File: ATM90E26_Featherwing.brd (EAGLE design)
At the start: 50.8 x 39.4 mm, 56 parts, among them J1 ST-PJ-312, J2 4P-SMD-2.0-90D, J3 4P-SMD-2.0-90D, J4 12V AC, Q1 8.192MHz, U1 ATM90E26, U2 CJT1117-5.0-SOT223

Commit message: Applied hackvana DRU
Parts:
- moved CS 0.25 mm to (3.30, 8.64)
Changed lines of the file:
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@@
 <?xml version="1.0" encoding="utf-8"?>
 <!DOCTYPE eagle SYSTEM "eagle.dtd">
-<eagle version="7.4.0">
+<eagle version="7.6.0">
 <drawing>
 <settings>
@@
 </class>
 </classes>
-<designrules name="OSHPark_2layer">
-<description language="de">&lt;b&gt;EAGLE Design Rules&lt;/b&gt;
+<designrules name="hackvana">
+<description language="de">&lt;b&gt;EAGLE Design Rules für Hackvana&lt;/b&gt;
 &lt;p&gt;
 Die Standard-Design-Rules sind so gewählt, dass sie für
@@
 Einstellungen hier und speichern die Design Rules unter
 einem neuen Namen ab.</description>
-<description language="en">&lt;b&gt;Laen's PCB Order Design Rules&lt;/b&gt;
+<description language="en">&lt;b&gt;EAGLE Design Rules for Hackvana&lt;/b&gt;
 &lt;p&gt;
-Please make sure your boards conform to these design rules.</description>
+The default Design Rules have been set to cover
+a wide range of applications. Your particular design
+may have different requirements, so please make the
+necessary adjustments and save your customized
+design rules under a new name.</description>
+<description language="zh">&lt;b&gt;EAGLE Design Rules for Hackvana&lt;/b&gt;
+</description>
 <param name="layerSetup" value="(1*16)"/>
-<param name="mtCopper" value="0.0356mm 0.0356mm 0.0356mm 0.0356mm 0.0356mm 0.0356mm 0.0356mm 0.0356mm 0.0356mm 0.0356mm 0.0356mm 0.0356mm 0.0356mm 0.0356mm 0.0356mm 0.0356mm"/>
-<param name="mtIsolate" value="1.5011mm 0.1499mm 0.2007mm 0.1499mm 0.2007mm 0.1499mm 0.2007mm 0.1499mm 0.2007mm 0.1499mm 0.2007mm 0.1499mm 0.2007mm 0.1499mm 0.2007mm"/>
+<param name="mtCopper" value="0.035mm 0.035mm 0.035mm 0.035mm 0.035mm 0.035mm 0.035mm 0.035mm 0.035mm 0.035mm 0.035mm 0.035mm 0.035mm 0.035mm 0.035mm 0.035mm"/>
+<param name="mtIsolate" value="1.5mm 0.15mm 0.2mm 0.15mm 0.2mm 0.15mm 0.2mm 0.15mm 0.2mm 0.15mm 0.2mm 0.15mm 0.2mm 0.15mm 0.2mm"/>
 <param name="mdWireWire" value="6mil"/>
 <param name="mdWirePad" value="6mil"/>
@@
 <param name="mdPadVia" value="6mil"/>
 <param name="mdViaVia" value="6mil"/>
-<param name="mdSmdPad" value="6mil"/>
-<param name="mdSmdVia" value="6mil"/>
-<param name="mdSmdSmd" value="6mil"/>
+<param name="mdSmdPad" value="0mil"/>
+<param name="mdSmdVia" value="0mil"/>
+<param name="mdSmdSmd" value="0mil"/>
 <param name="mdViaViaSameLayer" value="8mil"/>
 <param name="mnLayersViaInSmd" value="2"/>
-<param name="mdCopperDimension" value="15mil"/>
+<param name="mdCopperDimension" value="6mil"/>
 <param name="mdDrill" value="6mil"/>
 <param name="mdSmdStop" value="0mil"/>
 <param name="msWidth" value="6mil"/>
-<param name="msDrill" value="13mil"/>
-<param name="msMicroVia" value="13mil"/>
+<param name="msDrill" value="0.3mm"/>
+<param name="msMicroVia" value="0.25mm"/>
 <param name="msBlindViaRatio" value="0.5"/>
 <param name="rvPadTop" value="0.25"/>
@@
 <param name="rvMicroViaOuter" value="0.25"/>
 <param name="rvMicroViaInner" value="0.25"/>
-<param name="rlMinPadTop" value="7mil"/>
+<param name="rlMinPadTop" value="10mil"/>
 <param name="rlMaxPadTop" value="20mil"/>
-<param name="rlMinPadInner" value="7mil"/>
+<param name="rlMinPadInner" value="10mil"/>
 <param name="rlMaxPadInner" value="20mil"/>
-<param name="rlMinPadBottom" value="7mil"/>
+<param name="rlMinPadBottom" value="10mil"/>
 <param name="rlMaxPadBottom" value="20mil"/>
-<param name="rlMinViaOuter" value="7mil"/>
+<param name="rlMinViaOuter" value="6mil"/>
 <param name="rlMaxViaOuter" value="20mil"/>
-<param name="rlMinViaInner" value="7mil"/>
+<param name="rlMinViaInner" value="6mil"/>
 <param name="rlMaxViaInner" value="20mil"/>
 <param name="rlMinMicroViaOuter" value="4mil"/>
@@
 <param name="psTop" value="-1"/>
 <param name="psBottom" value="-1"/>
-<param name="psFirst" value="-1"/>
+<param name="psFirst" value="0"/>
 <param name="psElongationLong" value="100"/>
 <param name="psElongationOffset" value="100"/>
 <param name="mvStopFrame" value="1"/>
 <param name="mvCreamFrame" value="0"/>
-<param name="mlMinStopFrame" value="3mil"/>
-<param name="mlMaxStopFrame" value="3mil"/>
+<param name="mlMinStopFrame" value="2mil"/>
+<param name="mlMaxStopFrame" value="2mil"/>
 <param name="mlMinCreamFrame" value="0mil"/>
 <param name="mlMaxCreamFrame" value="0mil"/>
-<param name="mlViaStopLimit" value="20mil"/>
+<param name="mlViaStopLimit" value="100mil"/>
 <param name="srRoundness" value="0"/>
 <param name="srMinRoundness" value="0mil"/>
@@
 <param name="checkAngle" value="0"/>
 <param name="checkFont" value="1"/>
-<param name="checkRestrict" value="1"/>
+<param name="checkRestrict" value="0"/>
 <param name="useDiameter" value="13"/>
 <param name="maxErrors" value="50"/>
@@
 <attribute name="NAME" x="5.22" y="11.138" size="0.8" layer="26" font="vector" ratio="20" rot="MR180"/>
 </element>
-<element name="CS" library="wirepad" package="SMD1,27-2,54" value="WIREPADSMD1,27-254" x="3.302" y="8.382" smashed="yes" rot="MR90">
-<attribute name="VALUE" x="3.302" y="8.382" size="0.8" layer="28" rot="MR90"/>
-<attribute name="NAME" x="5.474" y="8.852" size="0.8" layer="26" font="vector" ratio="20" rot="MR180"/>
+<element name="CS" library="wirepad" package="SMD1,27-2,54" value="WIREPADSMD1,27-254" x="3.302" y="8.636" smashed="yes" rot="MR90">
+<attribute name="VALUE" x="3.302" y="8.636" size="0.8" layer="28" rot="MR90"/>
+<attribute name="NAME" x="5.474" y="9.106" size="0.8" layer="26" font="vector" ratio="20" rot="MR180"/>
 </element>
 <element name="C16" library="Discrete" package="C0603" value="100n" x="12.446" y="37.084" smashed="yes">
@@
 <wire x1="5.2832" y1="8.2296" x2="8.3312" y2="5.1816" width="0.254" layer="16"/>
 <wire x1="3.4544" y1="8.2296" x2="5.2832" y2="8.2296" width="0.254" layer="16"/>
-<wire x1="3.302" y1="8.382" x2="3.4544" y2="8.2296" width="0.254" layer="16"/>
+<wire x1="3.302" y1="8.636" x2="3.4544" y2="8.2296" width="0.254" layer="16"/>
 <wire x1="27.7368" y1="15.5448" x2="27.786" y2="15.595" width="0.254" layer="1"/>
 <via x="25.6032" y="11.3792" extent="1-16" drill="0.3302"/>

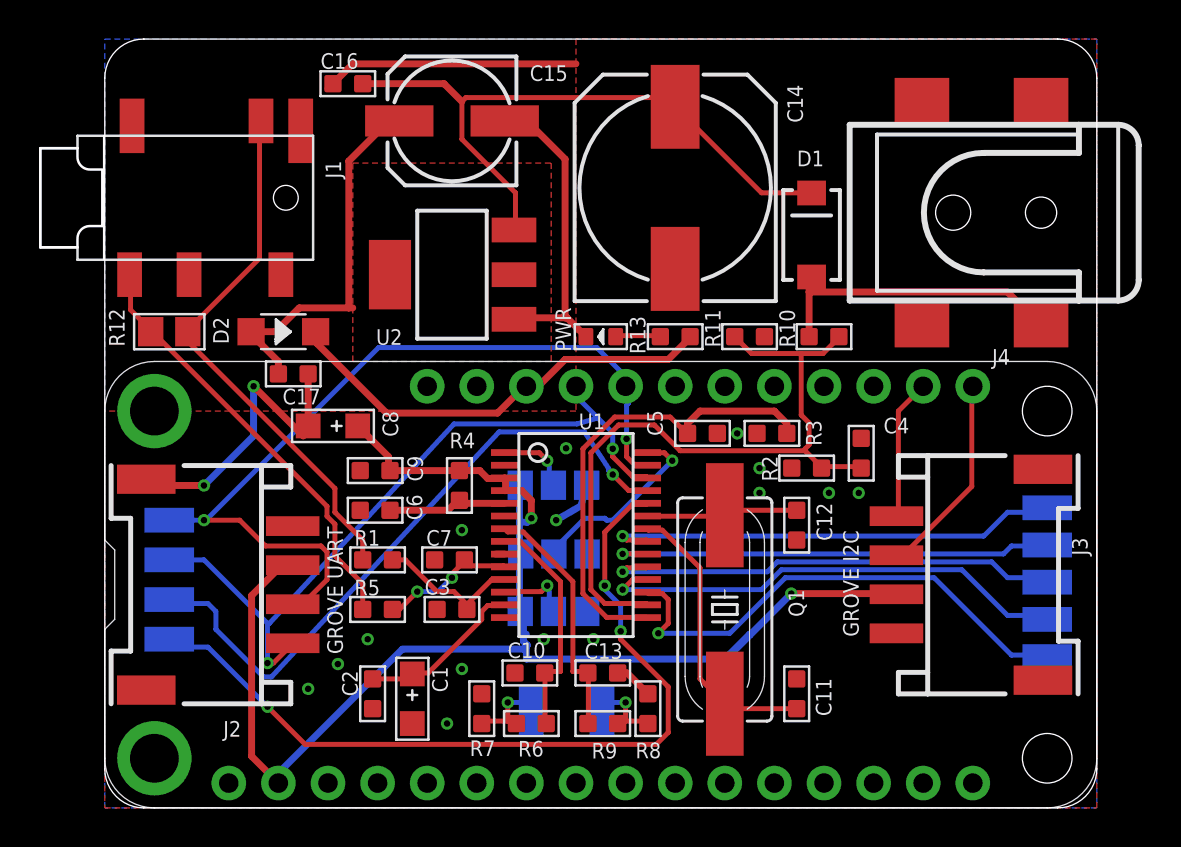
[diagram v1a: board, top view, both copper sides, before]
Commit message: Reduced size a bit to reduce cost
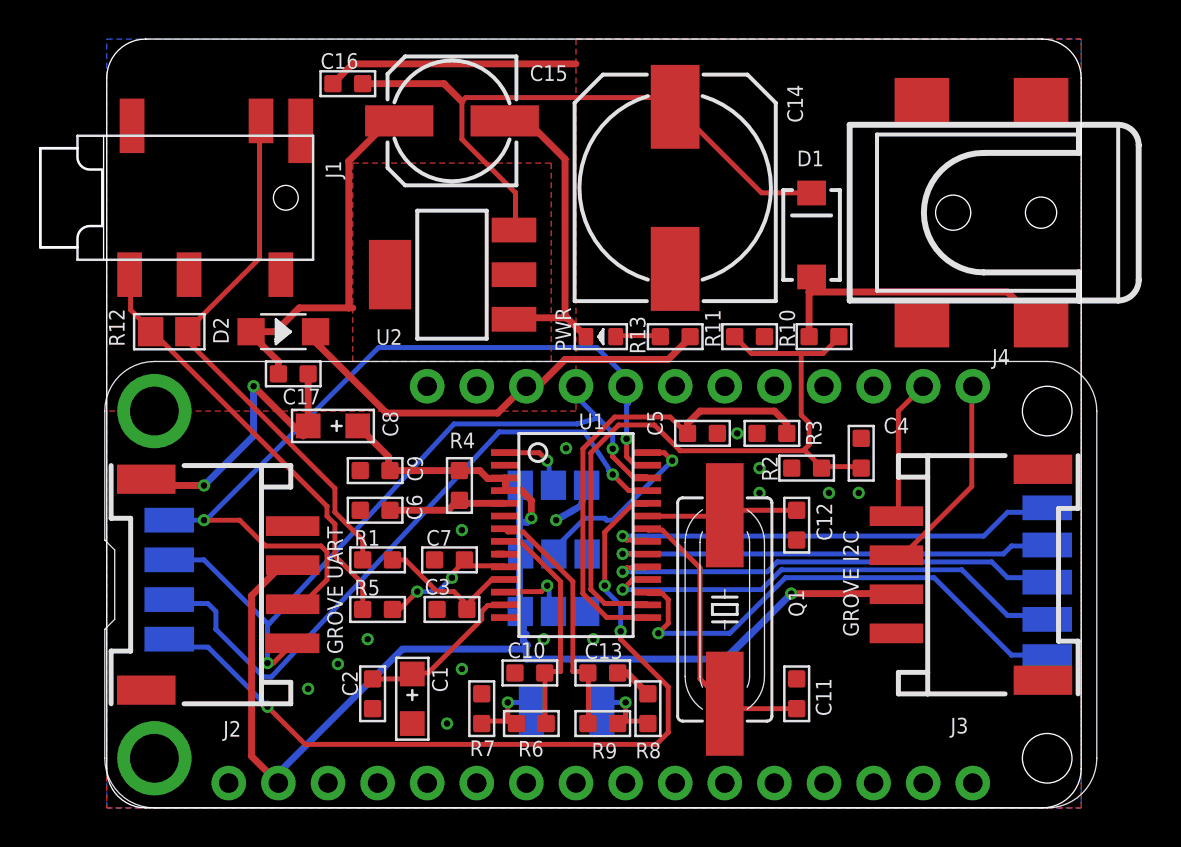
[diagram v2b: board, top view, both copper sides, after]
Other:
- board size 50.8 x 39.4 mm -> 49.9 x 39.4 mm
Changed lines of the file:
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@@
 <setting verticaltext="up"/>
 </settings>
-<grid distance="0.05" unitdist="inch" unit="mil" style="lines" multiple="1" display="no" altdistance="5" altunitdist="mil" altunit="mil"/>
+<grid distance="0.05" unitdist="inch" unit="mm" style="lines" multiple="1" display="no" altdistance="5" altunitdist="mil" altunit="mm"/>
 <layers>
 <layer number="1" name="Top" color="4" fill="1" visible="yes" active="yes"/>
@@
 <layer number="17" name="Pads" color="2" fill="1" visible="yes" active="yes"/>
 <layer number="18" name="Vias" color="2" fill="1" visible="yes" active="yes"/>
-<layer number="19" name="Unrouted" color="6" fill="1" visible="yes" active="yes"/>
+<layer number="19" name="Unrouted" color="6" fill="1" visible="no" active="yes"/>
 <layer number="20" name="Dimension" color="15" fill="1" visible="yes" active="yes"/>
 <layer number="21" name="tPlace" color="7" fill="1" visible="yes" active="yes"/>
@@
 <board>
 <plain>
-<wire x1="0" y1="2" x2="0" y2="37.37" width="0" layer="20"/>
-<wire x1="0" y1="37.37" x2="2" y2="39.37" width="0" layer="20" curve="-90"/>
-<wire x1="2" y1="39.37" x2="48.8" y2="39.37" width="0" layer="20"/>
-<wire x1="48.8" y1="39.37" x2="50.8" y2="37.37" width="0" layer="20" curve="-90"/>
-<wire x1="50.8" y1="37.37" x2="50.8" y2="2" width="0" layer="20"/>
-<wire x1="50.8" y1="2" x2="48.8" y2="0" width="0" layer="20" curve="-90"/>
-<wire x1="48.8" y1="0" x2="2" y2="0" width="0" layer="20"/>
-<wire x1="2" y1="0" x2="0" y2="2" width="0" layer="20" curve="-90"/>
+<wire x1="0.1" y1="2" x2="0.1" y2="37.37" width="0" layer="20"/>
+<wire x1="0.1" y1="37.37" x2="2.1" y2="39.37" width="0" layer="20" curve="-90"/>
+<wire x1="2.1" y1="39.37" x2="48" y2="39.37" width="0" layer="20"/>
+<wire x1="48" y1="39.37" x2="50" y2="37.37" width="0" layer="20" curve="-90"/>
+<wire x1="50" y1="37.37" x2="50" y2="2" width="0" layer="20"/>
+<wire x1="50" y1="2" x2="48" y2="0" width="0" layer="20" curve="-90"/>
+<wire x1="48" y1="0" x2="2.1" y2="0" width="0" layer="20"/>
+<wire x1="2.1" y1="0" x2="0.1" y2="2" width="0" layer="20" curve="-90"/>
 <text x="19.05" y="35.56" size="0.8" layer="22" font="vector" ratio="20">&gt;CNAME</text>
 <text x="22.86" y="34.29" size="0.8" layer="22" font="vector" ratio="20">&gt;DESIGNER</text>
@@
 </element>
 <element name="J3" library="Seeed-Connector -2016" package="HW4-SMD-2.0-90D" value="4P-SMD-2.0-90D" x="40.64" y="11.938" smashed="yes" rot="R270">
-<attribute name="NAME" x="49.53" y="13.843" size="0.8" layer="25" font="vector" ratio="20" rot="R270"/>
+<attribute name="NAME" x="43.307" y="3.81" size="0.8" layer="25" font="vector" ratio="20"/>
 <attribute name="VALUE" x="45.085" y="14.478" size="0.8" layer="27" font="vector" ratio="20" rot="R270"/>
 </element>
@@
 <contactref element="J2" pad="4"/>
 <polygon width="0.4064" layer="16">
-<vertex x="0" y="39.37"/>
-<vertex x="50.8" y="39.37"/>
-<vertex x="50.8" y="0"/>
-<vertex x="0" y="0"/>
+<vertex x="0.1" y="39.37"/>
+<vertex x="50" y="39.37"/>
+<vertex x="50" y="0"/>
+<vertex x="0.1" y="0"/>
 </polygon>
 <contactref element="J3" pad="SS2"/>
@@
 <contactref element="J3" pad="4"/>
 <polygon width="0.4064" layer="1">
-<vertex x="0" y="0"/>
-<vertex x="50.8" y="0"/>
-<vertex x="50.8" y="39.37"/>
+<vertex x="0.1" y="0"/>
+<vertex x="50" y="0"/>
+<vertex x="50" y="39.37"/>
 <vertex x="24.13" y="39.37"/>
 <vertex x="24.13" y="20.32"/>
-<vertex x="0" y="20.32"/>
+<vertex x="0.1" y="20.32"/>
 </polygon>
 <wire x1="23.6728" y1="25.0952" x2="23.5712" y2="25.0952" width="0.3556" layer="1"/>

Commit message: Finalised routing
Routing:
- net GND: track 50.4 -> 60.0 mm, vias 17 -> 24
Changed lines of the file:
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@@
 <?xml version="1.0" encoding="utf-8"?>
 <!DOCTYPE eagle SYSTEM "eagle.dtd">
-<eagle version="7.6.0">
+<eagle version="7.4.0">
 <drawing>
 <settings>
@@
 <setting verticaltext="up"/>
 </settings>
-<grid distance="0.05" unitdist="inch" unit="mm" style="lines" multiple="1" display="no" altdistance="5" altunitdist="mil" altunit="mm"/>
+<grid distance="0.05" unitdist="inch" unit="mil" style="lines" multiple="1" display="no" altdistance="5" altunitdist="mil" altunit="mil"/>
 <layers>
 <layer number="1" name="Top" color="4" fill="1" visible="yes" active="yes"/>
@@
 <layer number="17" name="Pads" color="2" fill="1" visible="yes" active="yes"/>
 <layer number="18" name="Vias" color="2" fill="1" visible="yes" active="yes"/>
-<layer number="19" name="Unrouted" color="6" fill="1" visible="no" active="yes"/>
+<layer number="19" name="Unrouted" color="6" fill="1" visible="yes" active="yes"/>
 <layer number="20" name="Dimension" color="15" fill="1" visible="yes" active="yes"/>
-<layer number="21" name="tPlace" color="7" fill="1" visible="yes" active="yes"/>
-<layer number="22" name="bPlace" color="13" fill="1" visible="yes" active="yes"/>
+<layer number="21" name="tPlace" color="7" fill="1" visible="no" active="yes"/>
+<layer number="22" name="bPlace" color="13" fill="1" visible="no" active="yes"/>
 <layer number="23" name="tOrigins" color="15" fill="1" visible="yes" active="yes"/>
 <layer number="24" name="bOrigins" color="15" fill="1" visible="yes" active="yes"/>
-<layer number="25" name="tNames" color="7" fill="1" visible="yes" active="yes"/>
-<layer number="26" name="bNames" color="13" fill="1" visible="yes" active="yes"/>
+<layer number="25" name="tNames" color="7" fill="1" visible="no" active="yes"/>
+<layer number="26" name="bNames" color="13" fill="1" visible="no" active="yes"/>
 <layer number="27" name="tValues" color="7" fill="1" visible="no" active="yes"/>
 <layer number="28" name="bValues" color="7" fill="1" visible="no" active="yes"/>
@@
 <wire x1="11.684" y1="37.084" x2="12.7" y2="38.1" width="0.3556" layer="1"/>
 <wire x1="11.43" y1="36.83" x2="11.684" y2="37.084" width="0.3556" layer="1"/>
+<wire x1="26.67" y1="25.4" x2="19.05" y2="25.4" width="0.4064" layer="16"/>
+<wire x1="20.32" y1="25.4" x2="19.05" y2="25.4" width="0.4064" layer="1"/>
+<wire x1="20.32" y1="25.4" x2="20.955" y2="25.019" width="0.4064" layer="1"/>
+<via x="19.05" y="25.4" extent="1-16" drill="0.3302"/>
+<via x="26.67" y="25.4" extent="1-16" drill="0.3302"/>
+<via x="26.67" y="33.02" extent="1-16" drill="0.3302"/>
+<via x="39.116" y="33.02" extent="1-16" drill="0.3302"/>
+<via x="38.989" y="37.719" extent="1-16" drill="0.3302"/>
+<via x="33.274" y="37.719" extent="1-16" drill="0.3302"/>
+<via x="33.274" y="33.274" extent="1-16" drill="0.3302"/>
 </signal>
 <signal name="+3V3" class="1">
